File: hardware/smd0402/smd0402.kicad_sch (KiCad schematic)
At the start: 33 parts, among them J1 Conn_01x04, J2 Conn_01x03, U1 WCH CH32V003F4U6

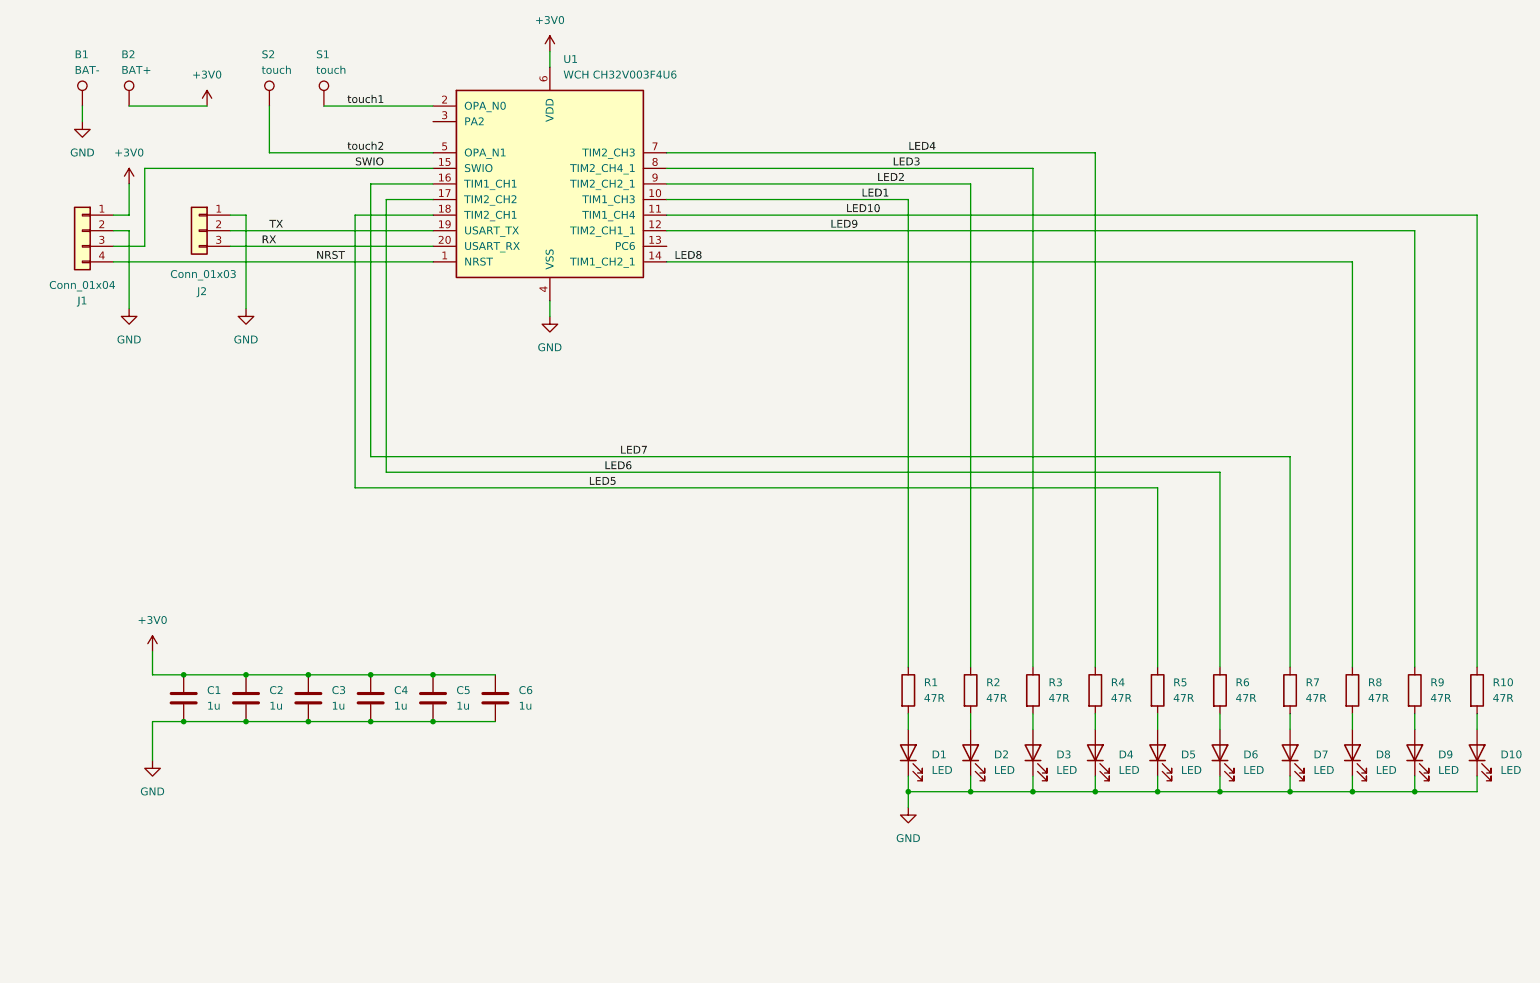
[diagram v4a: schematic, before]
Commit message: lose NRST, use TIM2 default mapping
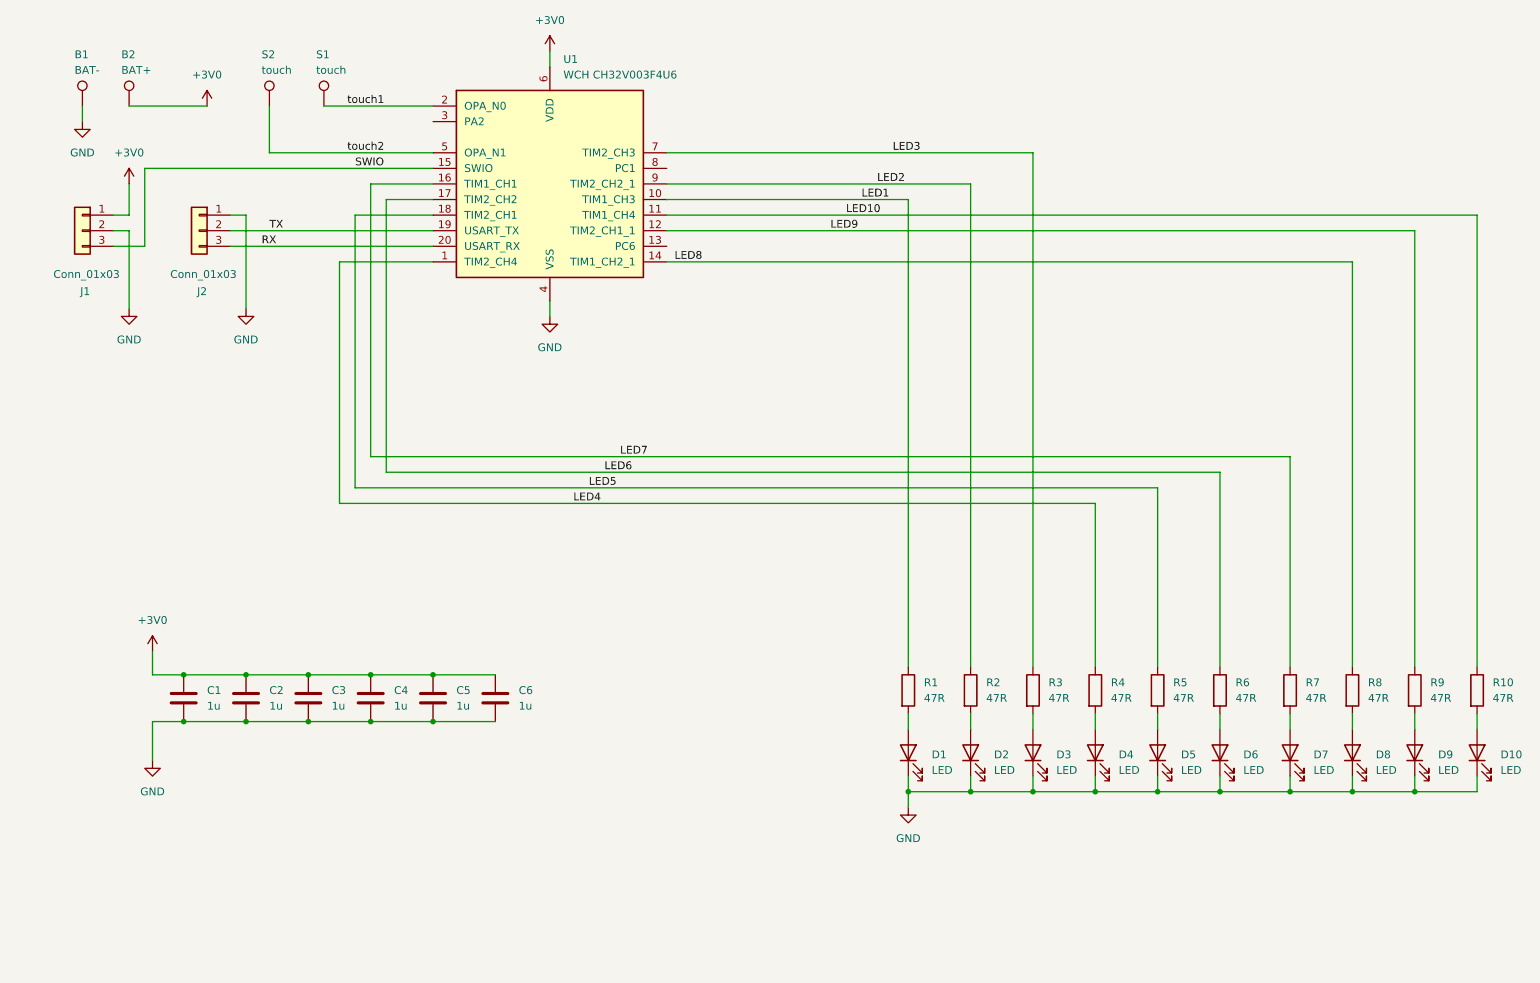
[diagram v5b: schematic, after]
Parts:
- removed J1: Conn_01x04, Connector_PinHeader_1.27mm:PinHeader_1x04_P1.27mm_Vertical, symbol Connector_Generic:Conn_01x04
- added J1: Conn_01x03, Connector_PinHeader_1.27mm:PinHeader_1x03_P1.27mm_Vertical, symbol Connector_Generic:Conn_01x03
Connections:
- net NRST is gone; now on net LED4: U1.1 (PD7)
- net +3V0: now also J1.1 (Pin_1)
- net GND: now also J1.2 (Pin_2)
- net LED3: now also U1.7 (PC0); no longer U1.8 (PC1)
- net LED4: no longer U1.7 (PC0)
- net SWIO: now also J1.3 (Pin_3)
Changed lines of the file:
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@@
 	(wire
 		(pts
+			(xy 196.85 114.3) (xy 73.66 114.3)
+		)
+		(stroke
+			(width 0)
+			(type default)
+		)
+	)
+	(wire
+		(pts
 			(xy 238.76 140.97) (xy 238.76 74.93)
 		)
@@
 	(wire
 		(pts
+			(xy 73.66 114.3) (xy 73.66 74.93)
+		)
+		(stroke
+			(width 0)
+			(type default)
+		)
+	)
+	(wire
+		(pts
 			(xy 58.42 142.24) (xy 68.58 142.24)
 		)
@@
 	(wire
 		(pts
-			(xy 196.85 57.15) (xy 127 57.15)
+			(xy 73.66 74.93) (xy 88.9 74.93)
 		)
 		(stroke
@@
 	(wire
 		(pts
-			(xy 186.69 59.69) (xy 127 59.69)
+			(xy 186.69 57.15) (xy 127 57.15)
 		)
 		(stroke
@@
 	(wire
 		(pts
+			(xy 196.85 114.3) (xy 196.85 140.97)
+		)
+		(stroke
+			(width 0)
+			(type default)
+		)
+	)
+	(wire
+		(pts
 			(xy 58.42 149.86) (xy 68.58 149.86)
 		)
@@
 	(wire
 		(pts
-			(xy 196.85 57.15) (xy 196.85 140.97)
-		)
-		(stroke
-			(width 0)
-			(type default)
-		)
-	)
-	(wire
-		(pts
 			(xy 43.18 138.43) (xy 43.18 142.24)
 		)
@@
 	(wire
 		(pts
-			(xy 36.83 74.93) (xy 88.9 74.93)
-		)
-		(stroke
-			(width 0)
-			(type default)
-		)
-	)
-	(wire
-		(pts
 			(xy 186.69 158.75) (xy 186.69 161.29)
 		)
@@
 	(wire
 		(pts
-			(xy 186.69 59.69) (xy 186.69 140.97)
+			(xy 186.69 57.15) (xy 186.69 140.97)
 		)
 		(stroke
@@
 	)
 	(label "LED4"
-		(at 166.37 57.15 0)
+		(at 111.76 114.3 0)
 		(effects
 			(font
@@
 		)
 	)
-	(label "NRST"
-		(at 69.85 74.93 0)
-		(effects
-			(font
-				(size 1.27 1.27)
-			)
-			(justify left bottom)
-		)
-	)
 	(label "SWIO"
 		(at 76.2 59.69 0)
@@
 	)
 	(label "LED3"
-		(at 163.83 59.69 0)
+		(at 163.83 57.15 0)
 		(effects
 			(font
@@
 	)
 	(symbol
-		(lib_id "Connector_Generic:Conn_01x04")
-		(at 31.75 69.85 0)
-		(mirror y)
-		(unit 1)
-		(exclude_from_sim no)
-		(in_bom no)
-		(on_board yes)
-		(dnp no)
-		(property "Reference" "J1"
-			(at 31.75 81.28 0)
-			(effects
-				(font
-					(size 1.27 1.27)
-				)
-			)
-		)
-		(property "Value" "Conn_01x04"
-			(at 31.75 78.74 0)
-			(effects
-				(font
-					(size 1.27 1.27)
-				)
-			)
-		)
-		(property "Footprint" "Connector_PinHeader_1.27mm:PinHeader_1x04_P1.27mm_Vertical"
-			(at 31.75 69.85 0)
-			(effects
-				(font
-					(size 1.27 1.27)
-				)
-				(hide yes)
-			)
-		)
-		(property "Datasheet" "~"
-			(at 31.75 69.85 0)
-			(effects
-				(font
-					(size 1.27 1.27)
-				)
-				(hide yes)
-			)
-		)
-		(property "Description" "Generic connector, single row, 01x04, script generated (kicad-library-utils/schlib/autogen/connector/)"
-			(at 31.75 69.85 0)
-			(effects
-				(font
-					(size 1.27 1.27)
-				)
-				(hide yes)
-			)
-		)
-		(property "JLC" ""
-			(at 31.75 69.85 0)
-			(effects
-				(font
-					(size 1.27 1.27)
-				)
-				(hide yes)
-			)
-		)
-		(pin "2"
-		)
-		(pin "1"
-		)
-		(pin "4"
-		)
-		(pin "3"
-		)
-		(instances
-			(project ""
-				(path "/b4d6c274-8f02-467a-b6b3-fe4c47a31499"
-					(reference "J1")
-					(unit 1)
-				)
-			)
-		)
-	)
-	(symbol
 		(lib_id "power:GND")
 		(at 107.95 83.82 0)
@@
 		)
 		(pin "8"
-			(alternate "TIM2_CH4_1")
 		)
 		(pin "21"
@@
 		)
 		(pin "1"
-			(alternate "NRST")
+			(alternate "TIM2_CH4")
 		)
 		(pin "10"
@@
 					(unit 1)
 				)
+			)
+		)
+	)
+	(symbol
+		(lib_id "Connector_Generic:Conn_01x03")
+		(at 31.75 69.85 0)
+		(mirror y)
+		(unit 1)
+		(exclude_from_sim no)
+		(in_bom no)
+		(on_board yes)
+		(dnp no)
+		(property "Reference" "J1"
+			(at 33.02 79.756 0)
+			(effects
+				(font
+					(size 1.27 1.27)
+				)
+				(justify left)
+			)
+		)
+		(property "Value" "Conn_01x03"
+			(at 37.846 76.962 0)
+			(effects
+				(font
+					(size 1.27 1.27)
+				)
+				(justify left)
+			)
+		)
+		(property "Footprint" "Connector_PinHeader_1.27mm:PinHeader_1x03_P1.27mm_Vertical"
+			(at 31.75 69.85 0)
+			(effects
+				(font
+					(size 1.27 1.27)
+				)
+				(hide yes)
+			)
+		)
+		(property "Datasheet" "~"
+			(at 31.75 69.85 0)
+			(effects
+				(font
+					(size 1.27 1.27)
+				)
+				(hide yes)
+			)
+		)
+		(property "Description" "Generic connector, single row, 01x03, script generated (kicad-library-utils/schlib/autogen/connector/)"
+			(at 31.75 69.85 0)
+			(effects
+				(font
+					(size 1.27 1.27)
+				)
+				(hide yes)
+			)
+		)
+		(property "JLC" ""
+			(at 31.75 69.85 0)
+			(effects
+				(font
+					(size 1.27 1.27)
+				)
+				(hide yes)
+			)
+		)
+		(pin "3"
+		)
+		(pin "2"
+		)
+		(pin "1"
+		)
+		(instances
+			(project "smd0402"
+				(path "/b4d6c274-8f02-467a-b6b3-fe4c47a31499"
+					(reference "J1")
+					(unit 1)
+				)

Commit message: boost dia to 50mm, use back-to-back LEDs, add SAO
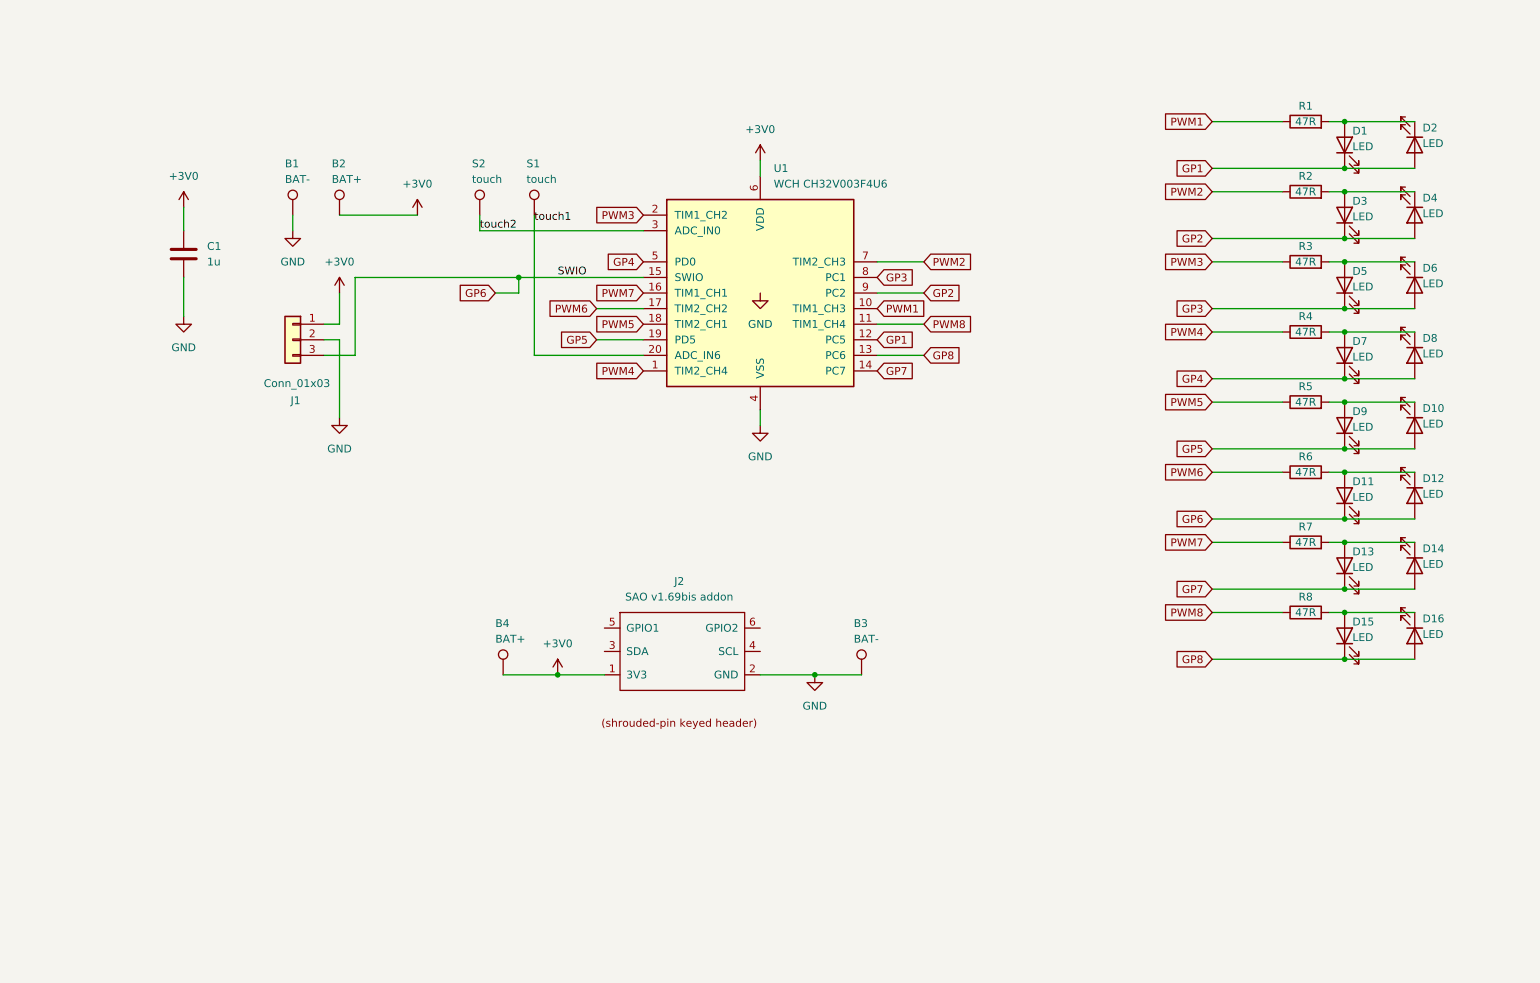
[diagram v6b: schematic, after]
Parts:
- removed C2, C3, C4, C5, C6: 1u, Capacitor_SMD:C_0402_1005Metric, symbol Device:C
- removed J2: Conn_01x03, Connector_PinHeader_1.27mm:PinHeader_1x03_P1.27mm_Vertical, symbol Connector_Generic:Conn_01x03
- removed R10, R9: 47R, Resistor_SMD:R_0402_1005Metric, symbol Device:R
- added B3: BAT-, TestPoint:TestPoint_Pad_D4.0mm, symbol Connector:TestPoint
- added B4: BAT+, TestPoint:TestPoint_Pad_D4.0mm, symbol Connector:TestPoint
- added D11, D12, D13, D14, D15, D16: LED, LED_SMD:LED_0402_1005Metric, symbol Device:LED
- added J2: SAO v1.69bis addon, Connector_IDC:IDC-Header_2x03_P2.54mm_Vertical, symbol extra:SAO v1.69bis addon
- D1, R1: JLC 0402 -> (none)
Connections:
- net LED9 is gone; now on net GP1: U1.12 (PC5)
- net RX is gone; now on net touch1: U1.20 (PD6)
- net TX is gone; now on net GP5: U1.19 (PD5)
- net VSS is gone; now on net GND: U1.21 (VSS)
- net +3V0: now also B4.1, J2.1 (3V3)
- net GND: now also B3.1, J2.2 (GND); no longer D1.1 (K), D10.1 (K), D2.1 (K), D3.1 (K), D4.1 (K), D5.1 (K), D6.1 (K), D7.1 (K), D8.1 (K), D9.1 (K)
- net touch1: no longer U1.2 (PA1)
- net touch2: now also U1.3 (PA2); no longer U1.5 (PD0)
- net at R4.2: now also D7.2 (A), D8.1 (K); no longer D4.2 (A)
- net at D3.2 (A): now also D4.1 (K), R2.2; no longer R3.2
- net at D9.2 (A): now also D10.1 (K), R5.2
- net at R6.2: now also D11.2 (A), D12.1 (K); no longer D6.2 (A)
- net GP5: now reaches D10.2 (A)
- net GP5: now also D9.1 (K)
- net at R8.2: now also D15.2 (A), D16.1 (K); no longer D8.2 (A)
- net at R7.2: now also D13.2 (A), D14.1 (K); no longer D7.2 (A)
- net at D1.2 (A), R1.2: now also D2.1 (K)
- net at D5.2 (A): now also D6.1 (K), R3.2; no longer R5.2
- net GP1: now reaches D2.2 (A)
- net GP1: now also D1.1 (K); no longer R2.2
- net GP8: now reaches U1.13 (PC6)
- net GP8: now also D15.1 (K), D16.2 (A)
- net GP3: now reaches U1.8 (PC1)
- net GP3: now also D5.1 (K), D6.2 (A)
- net LED1 renamed PWM1
- net LED10 renamed PWM8
- net PWM8: now also R8.1
- net LED2 renamed GP2
- net GP2: now also D3.1 (K), D4.2 (A); no longer R2.1
- net LED3 renamed PWM2
- net PWM2: now also R2.1; no longer R3.1
- net LED4 renamed PWM4
- net LED5 renamed PWM5
- net LED6 renamed PWM6
- net LED7 renamed PWM7
- net LED8 renamed GP7
- net GP7: now also D13.1 (K), D14.2 (A); no longer R8.1
- net SWIO renamed GP6
- net GP6: now also D11.1 (K), D12.2 (A)
- new net GP4: D7.1 (K), D8.2 (A), U1.5 (PD0)
- new net PWM3: R3.1, U1.2 (PA1)
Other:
- moved on the sheet: B1, B2, C1, D10, D2, D3, D4, D5, D6, D7, D8, D9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

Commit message: add SAO display board
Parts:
- added J3: SAO v1.69bis badge, Connector_IDC:IDC-Header_2x03_P2.54mm_Vertical, symbol extra:SAO v1.69bis badge
- added P1, P2, P3, P4, P5, P6: Conn_01x02, Connector_PinHeader_2.54mm:PinHeader_1x02_P2.54mm_Vertical, symbol Connector_Generic:Conn_01x02
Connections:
- net +3V0: now also J3.5 (3V3), P1.1 (Pin_1), P2.1 (Pin_1), P3.1 (Pin_1), P4.1 (Pin_1), P5.1 (Pin_1), P6.1 (Pin_1)
- net GND: now also J3.6 (GND), P1.2 (Pin_2), P2.2 (Pin_2), P3.2 (Pin_2), P4.2 (Pin_2), P5.2 (Pin_2), P6.2 (Pin_2)
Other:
- moved on the sheet: B3, B4, J2
